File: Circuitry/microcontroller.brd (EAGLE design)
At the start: 100 x 80 mm, 0 parts

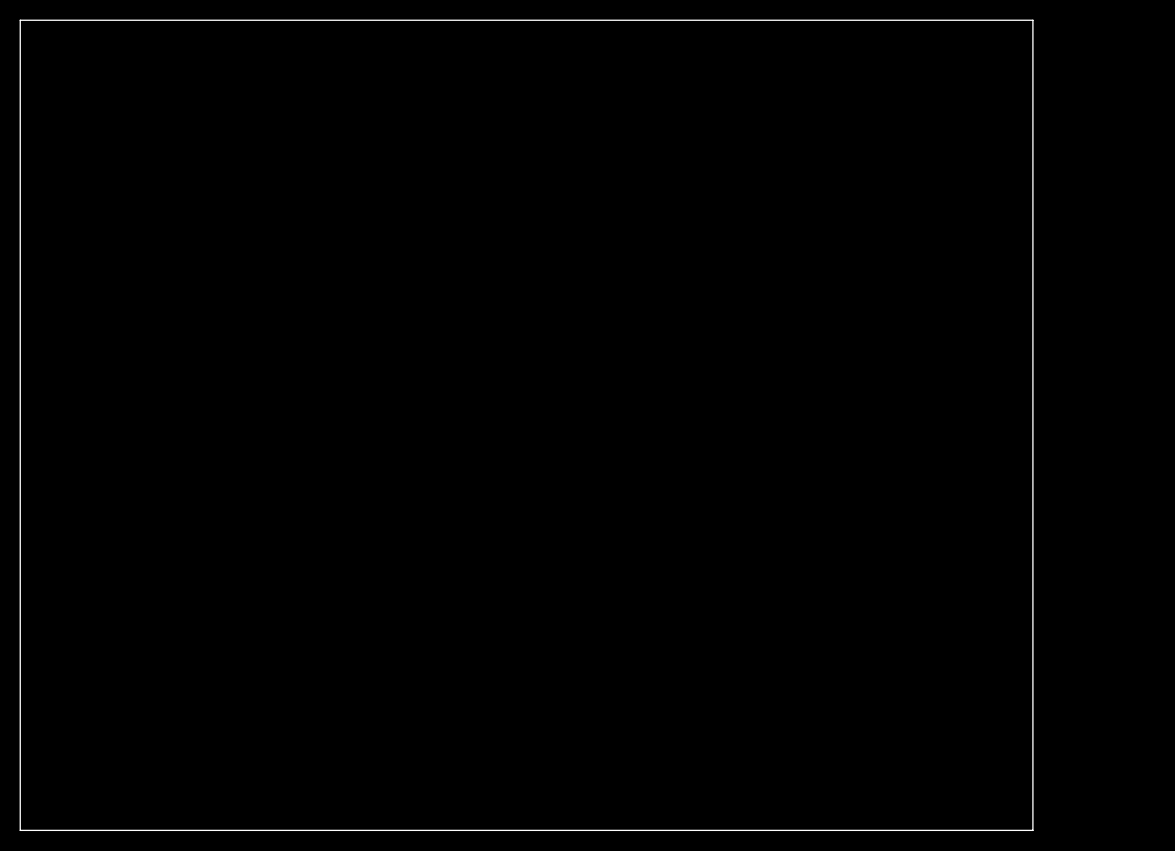
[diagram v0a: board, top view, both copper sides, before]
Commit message: add connections between components
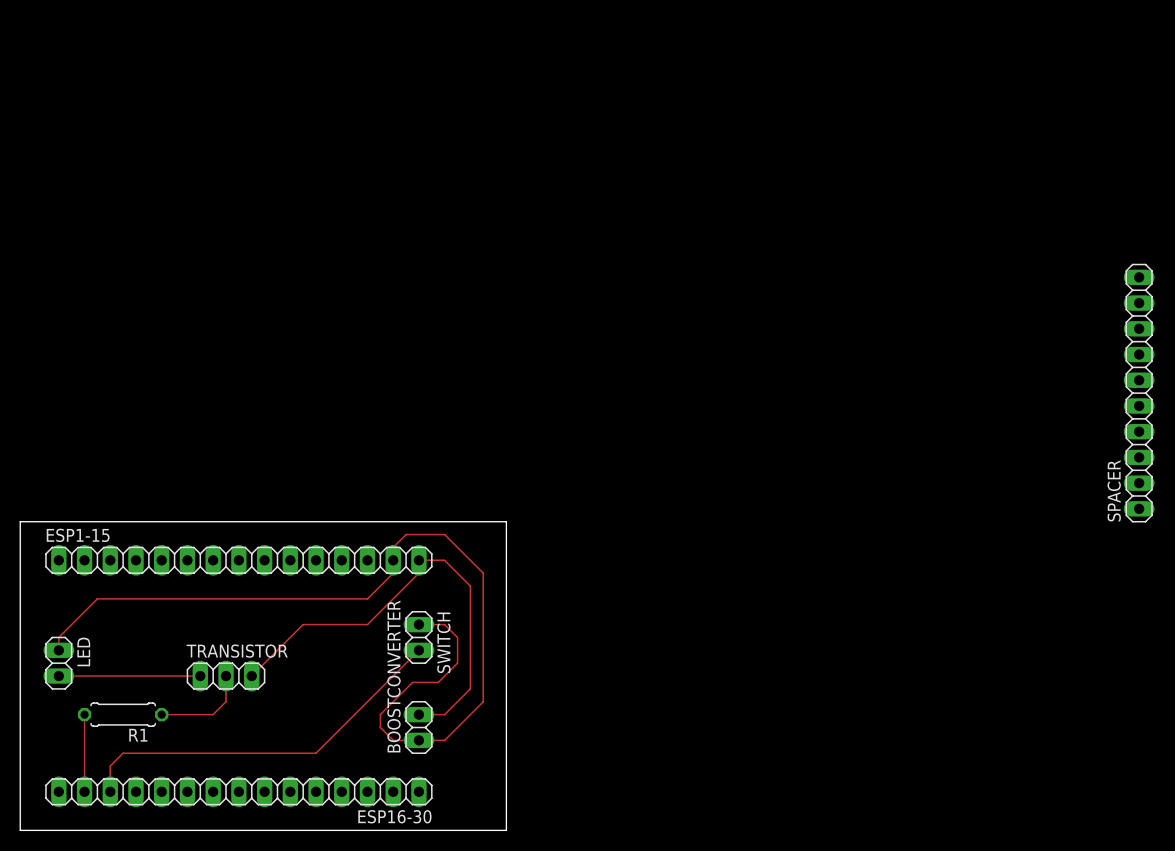
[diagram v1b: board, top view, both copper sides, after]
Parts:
- added BOOSTCONVERTER, LED, SWITCH: (no value), pinhead:1X02
- added ESP1-15, ESP16-30: (no value), pinhead:1X15
- added R1: (no value), rcl:0207/7
- added SPACER: (no value), pinhead:1X10
- added TRANSISTOR: (no value), pinhead:1X03
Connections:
- new net N$1: BOOSTCONVERTER.1, ESP1-15.14, LED.1, SWITCH.1
- new net N$2: BOOSTCONVERTER.2, ESP1-15.15, TRANSISTOR.3
- new net N$3: R1.1, TRANSISTOR.2
- new net N$4: ESP16-30.14, R1.2
- new net N$5: ESP16-30.13, SWITCH.2
- new net N$6: LED.2, TRANSISTOR.1
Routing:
- net N$1: track 0.00 -> 94.6 mm
- net N$2: track 0.00 -> 44.4 mm
- net N$5: track 0.00 -> 37.8 mm
- net N$6: track 0.00 -> 14.0 mm
- net N$3: track 0.00 -> 9.42 mm
- net N$4: track 0.00 -> 7.62 mm
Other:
- board size 100 x 80 mm -> 48 x 30.5 mm

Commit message: fix the microcontroller board
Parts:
- removed SPACER: (no value), pinhead:1X10
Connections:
- net N$1: now also TRANSISTOR.3; no longer LED.1
- net N$2: now also LED.1; no longer TRANSISTOR.3
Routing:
- net N$1: track 94.6 -> 75.0 mm
- net N$2: track 44.4 -> 62.4 mm
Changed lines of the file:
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@@
 <attribute name="VALUE" x="40.64" y="6.985" size="1.27" layer="27" rot="R180"/>
-</element>
-<element name="SPACER" library="pinhead" library_urn="urn:adsk.eagle:library:325" package="1X10" package3d_urn="urn:adsk.eagle:package:22406/2" value="" x="110.49" y="43.18" smashed="yes" rot="R90">
-<attribute name="NAME" x="108.6612" y="30.4038" size="1.27" layer="25" ratio="10" rot="R90"/>
-<attribute name="POPULARITY" value="35" x="110.49" y="43.18" size="1.778" layer="27" rot="R90" display="off"/>
-<attribute name="VALUE" x="113.665" y="30.48" size="1.27" layer="27" rot="R90"/>
 </element>
 <element name="R1" library="rcl" library_urn="urn:adsk.eagle:library:334" package="0207/7" package3d_urn="urn:adsk.eagle:package:23493/2" value="" x="10.16" y="11.43" smashed="yes" rot="R180">
@@
 <signals>
 <signal name="N$1">
-<contactref element="LED" pad="1"/>
 <contactref element="SWITCH" pad="1"/>
 <contactref element="BOOSTCONVERTER" pad="1"/>
@@
 <wire x1="41.91" y1="8.89" x2="45.72" y2="12.7" width="0.1524" layer="1"/>
 <wire x1="45.72" y1="12.7" x2="45.72" y2="25.4" width="0.1524" layer="1"/>
-<wire x1="3.81" y1="17.78" x2="3.81" y2="19.05" width="0.1524" layer="1"/>
-<wire x1="3.81" y1="19.05" x2="7.62" y2="22.86" width="0.1524" layer="1"/>
-<wire x1="7.62" y1="22.86" x2="34.29" y2="22.86" width="0.1524" layer="1"/>
-<wire x1="34.29" y1="22.86" x2="36.83" y2="25.4" width="0.1524" layer="1"/>
-<wire x1="36.83" y1="25.4" x2="36.83" y2="26.67" width="0.1524" layer="1"/>
 <wire x1="35.56" y1="11.43" x2="35.56" y2="10.16" width="0.1524" layer="1"/>
 <wire x1="35.56" y1="10.16" x2="36.83" y2="8.89" width="0.1524" layer="1"/>
@@
 <wire x1="38.1" y1="29.21" x2="41.91" y2="29.21" width="0.1524" layer="1"/>
 <wire x1="41.91" y1="29.21" x2="45.72" y2="25.4" width="0.1524" layer="1"/>
+<contactref element="TRANSISTOR" pad="3"/>
+<wire x1="22.86" y1="15.24" x2="33.02" y2="15.24" width="0.1524" layer="1"/>
+<wire x1="38.1" y1="20.32" x2="39.37" y2="20.32" width="0.1524" layer="1"/>
+<wire x1="33.02" y1="15.24" x2="38.1" y2="20.32" width="0.1524" layer="1"/>
 </signal>
 <signal name="N$2">
 <contactref element="ESP1-15" pad="15"/>
-<contactref element="TRANSISTOR" pad="3"/>
 <contactref element="BOOSTCONVERTER" pad="2"/>
-<wire x1="22.86" y1="15.24" x2="27.94" y2="20.32" width="0.1524" layer="1"/>
-<wire x1="27.94" y1="20.32" x2="34.29" y2="20.32" width="0.1524" layer="1"/>
 <wire x1="39.37" y1="25.4" x2="39.37" y2="26.67" width="0.1524" layer="1"/>
-<wire x1="39.37" y1="25.4" x2="34.29" y2="20.32" width="0.1524" layer="1"/>
+<wire x1="39.37" y1="25.4" x2="35.56" y2="21.59" width="0.1524" layer="1"/>
 <wire x1="39.37" y1="11.43" x2="41.91" y2="11.43" width="0.1524" layer="1"/>
 <wire x1="41.91" y1="11.43" x2="44.45" y2="13.97" width="0.1524" layer="1"/>
@@
 <wire x1="44.45" y1="24.13" x2="41.91" y2="26.67" width="0.1524" layer="1"/>
 <wire x1="41.91" y1="26.67" x2="39.37" y2="26.67" width="0.1524" layer="1"/>
+<contactref element="LED" pad="1"/>
+<wire x1="3.81" y1="17.78" x2="7.62" y2="21.59" width="0.1524" layer="1"/>
+<wire x1="7.62" y1="21.59" x2="35.56" y2="21.59" width="0.1524" layer="1"/>
 </signal>
 <signal name="N$3">

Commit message: add initial components and header pins to board
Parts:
- removed BOOSTCONVERTER, LED, SWITCH: (no value), pinhead:1X02
- removed ESP1-15, ESP16-30: (no value), pinhead:1X15
- removed R1: (no value), rcl:0207/7
- removed TRANSISTOR: (no value), pinhead:1X03
- added BAT_READ, TRIGGER: (no value), pinhead:1X01
- added IR_LED, OLED, PWR: (no value), pinhead:1X02
- added IR_TRS: 2N5088, transistor-npn:TO92
- added JP3, JP4: (no value), pinhead:1X15
- added LED_CTRL: (no value), pinhead:1X04
- added SHIFT_REG: (no value), pinhead:1X05
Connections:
- removed net N$2: BOOSTCONVERTER.2, ESP1-15.15, LED.1
- removed net N$3: R1.1, TRANSISTOR.2
- removed net N$4: ESP16-30.14, R1.2
- removed net N$5: ESP16-30.13, SWITCH.2
- removed net N$6: LED.2, TRANSISTOR.1
- new net 0: IR_LED.2, JP3.14, LED_CTRL.4, PWR.2, SHIFT_REG.5
- new net BATTERY_CHECKER: BAT_READ.1, JP3.1
- new net B_CTRL: JP4.13, LED_CTRL.3
- new net CLOCK: JP4.8, SHIFT_REG.3
- new net DATA: JP4.5, SHIFT_REG.2
- new net G_CTRL: JP4.11, LED_CTRL.2
- new net IR_LED: IR_TRS.2, JP4.4
- new net LATCH: JP4.9, SHIFT_REG.4
- new net OLED_SCL_PIN: JP4.2, OLED.1
- new net OLED_SDA: JP4.3, OLED.2
- new net R_CTRL: JP4.10, LED_CTRL.1
- new net TRIGGER: JP4.1, TRIGGER.1
- new net VCC: IR_TRS.1, JP3.15, PWR.1, SHIFT_REG.1
- net N$1: now also IR_LED.1, IR_TRS.3; no longer BOOSTCONVERTER.1, ESP1-15.14, SWITCH.1, TRANSISTOR.3
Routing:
- net N$1: track 75.0 -> 0.00 mm
- net N$2: track 62.4 -> 0.00 mm
- net N$5: track 37.8 -> 0.00 mm
- net N$6: track 14.0 -> 0.00 mm
- net N$3: track 9.42 -> 0.00 mm
- net N$4: track 7.62 -> 0.00 mm
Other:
- board size 48 x 30.5 mm -> 160 x 100 mm

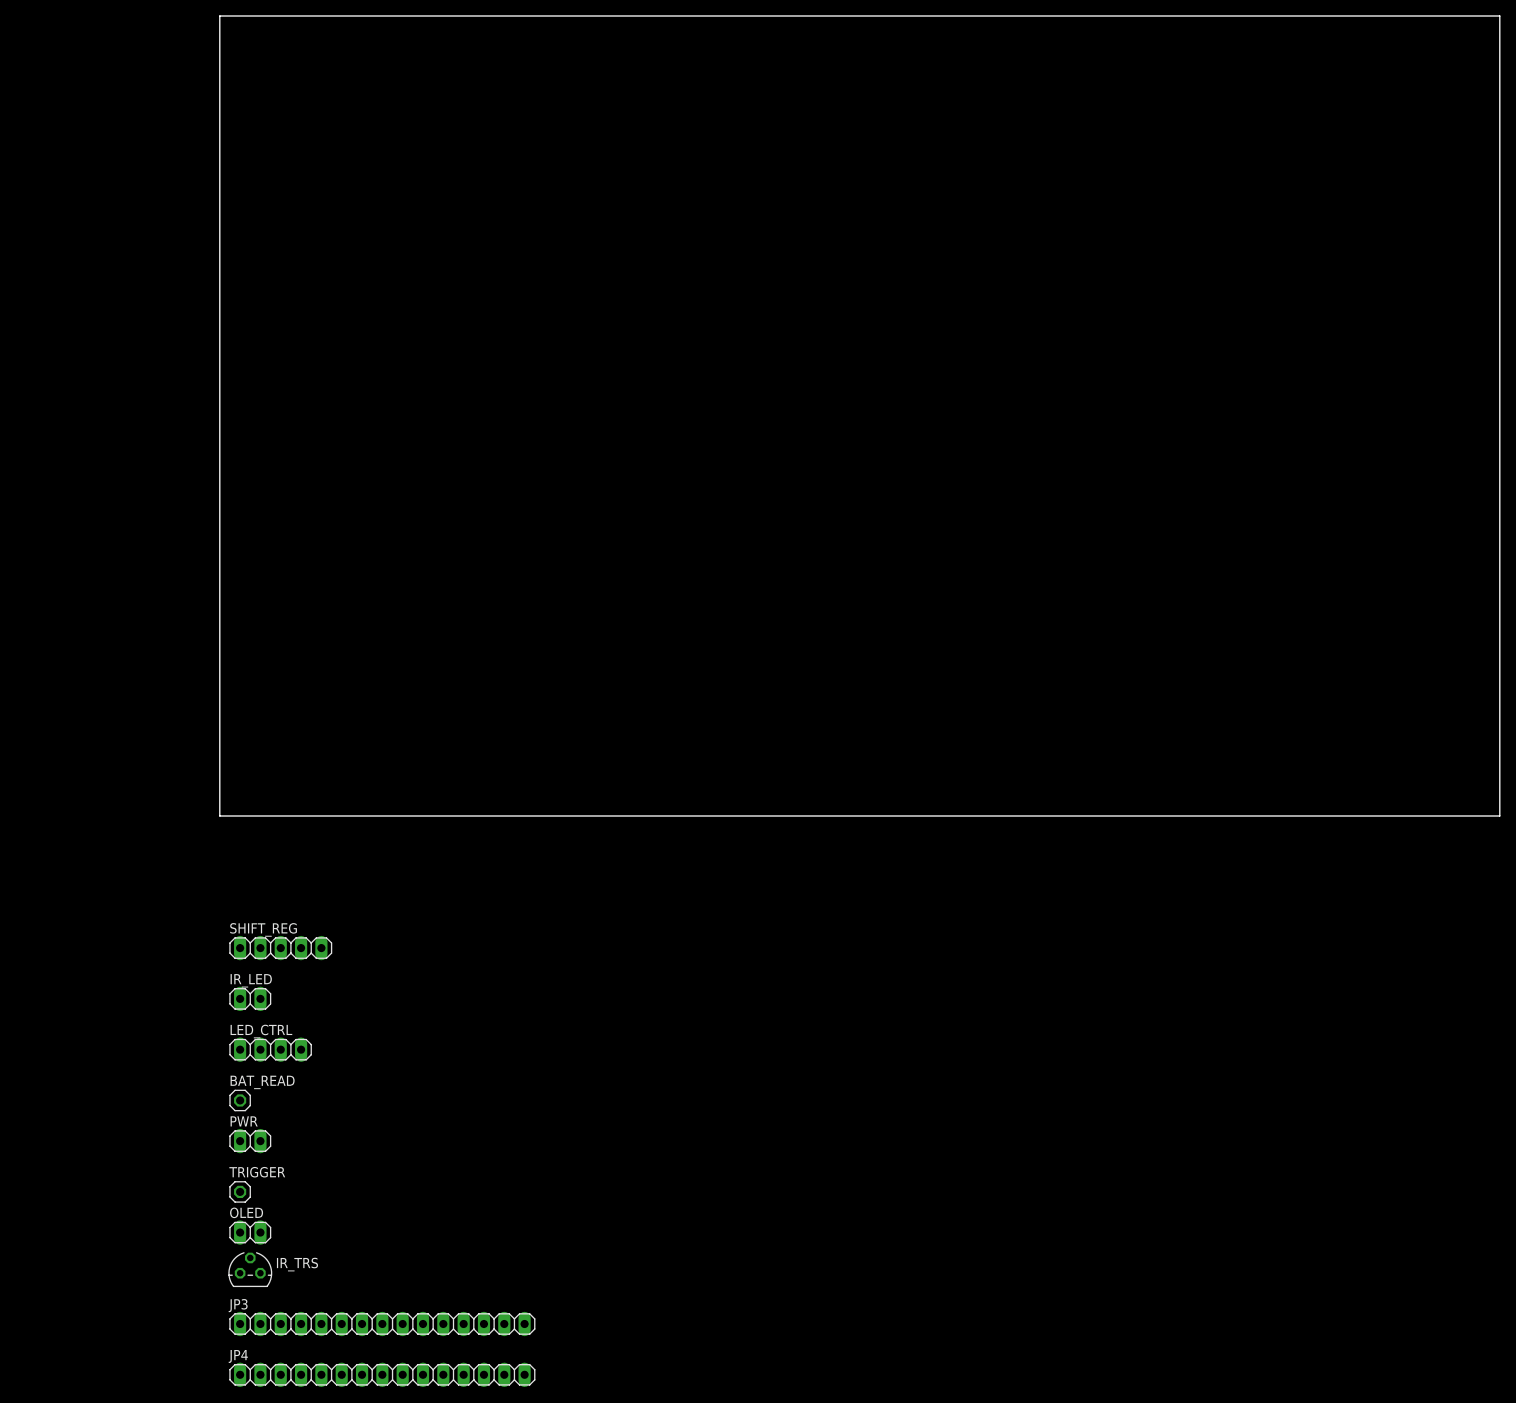
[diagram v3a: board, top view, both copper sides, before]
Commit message: create microcontroller board
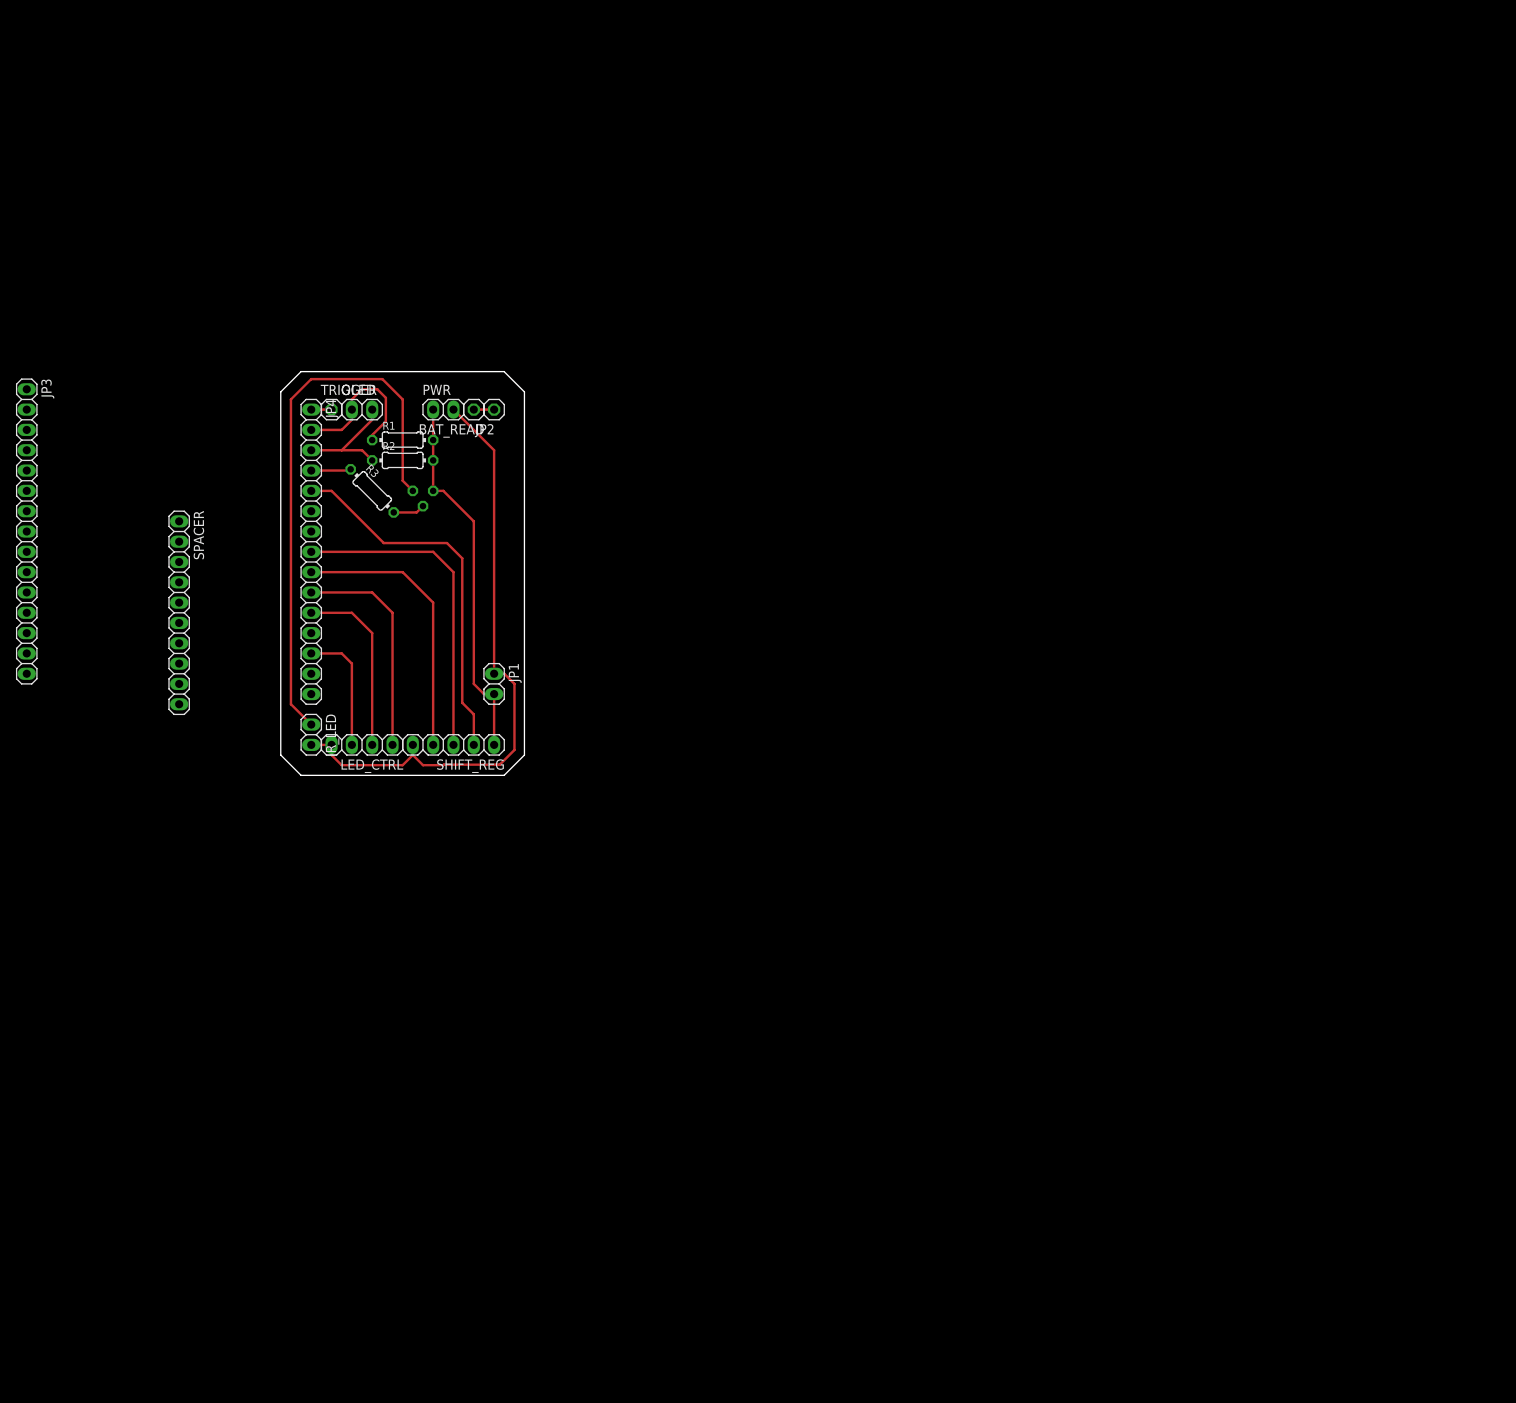
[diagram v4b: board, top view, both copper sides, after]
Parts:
- added JP1: (no value), pinhead:1X02
- added JP2: (no value), pinhead:1X01
- added R1, R2: 10k, rcl:0204/7
- added R3: (no value), rcl:0204/7
- added SPACER: (no value), pinhead:1X10
- moved JP3 108.6 mm to (-24.1, 35.6), turned to 270 degrees
- moved OLED 103.8 mm to (17.8, 50.8)
- moved JP4 103.3 mm to (11.4, 33.0), turned to 270 degrees
- moved IR_TRS 100.1 mm to (25.4, 40.6), flipped to the bottom, turned to 180 degrees
- moved TRIGGER 98.5 mm to (14.0, 50.8)
- moved PWR 94.6 mm to (27.9, 50.8)
- moved BAT_READ 91.2 mm to (31.8, 50.8), turned to 180 degrees
- moved LED_CTRL 39.8 mm to (17.8, 8.89), turned to 180 degrees
- moved IR_LED 33.9 mm to (11.4, 10.2), turned to 270 degrees
- moved SHIFT_REG 33.3 mm to (29.2, 8.89), turned to 180 degrees
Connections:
- new net N$2: IR_TRS.2, R3.2
- net 0: now also JP1.1; no longer JP3.14
- net BATTERY_CHECKER: now also JP2.1; no longer JP3.1
- net IR_LED: now also R3.1; no longer IR_TRS.2
- net OLED_SCL_PIN: now also R1.1
- net OLED_SDA: now also R2.1
- net VCC: now also JP1.2, R1.2, R2.2; no longer JP3.15
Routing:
- net 0: track 0.00 -> 76.8 mm
- net N$1: track 0.00 -> 69.7 mm
- net VCC: track 0.00 -> 46.6 mm
- net DATA: track 0.00 -> 46.3 mm
- net CLOCK: track 0.00 -> 40.4 mm
- net LATCH: track 0.00 -> 34.6 mm
- net R_CTRL: track 0.00 -> 27.7 mm
- net G_CTRL: track 0.00 -> 22.6 mm
- net OLED_SCL_PIN: track 0.00 -> 19.4 mm
- net B_CTRL: track 0.00 -> 15.8 mm
- net OLED_SDA: track 0.00 -> 14.8 mm
- net IR_LED: track 0.00 -> 4.99 mm
- net N$2: track 0.00 -> 3.98 mm
- net TRIGGER: track 0.00 -> 2.54 mm
- net BATTERY_CHECKER: track 0.00 -> 2.54 mm
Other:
- board size 160 x 100 mm -> 30.5 x 50.5 mm
